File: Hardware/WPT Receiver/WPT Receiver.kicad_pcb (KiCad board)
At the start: 2 copper layers, 100 x 100 mm, 158 parts, among them J1 0.1" Header, J2 Tag-connect-NL, J3 0.1" Header, J4 0.1" Header, SW1 PTS647, SW2 PTS647, SW3 PTS647, U1 STM32G031C6U6, U10 74HC595, U2 INA180A3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

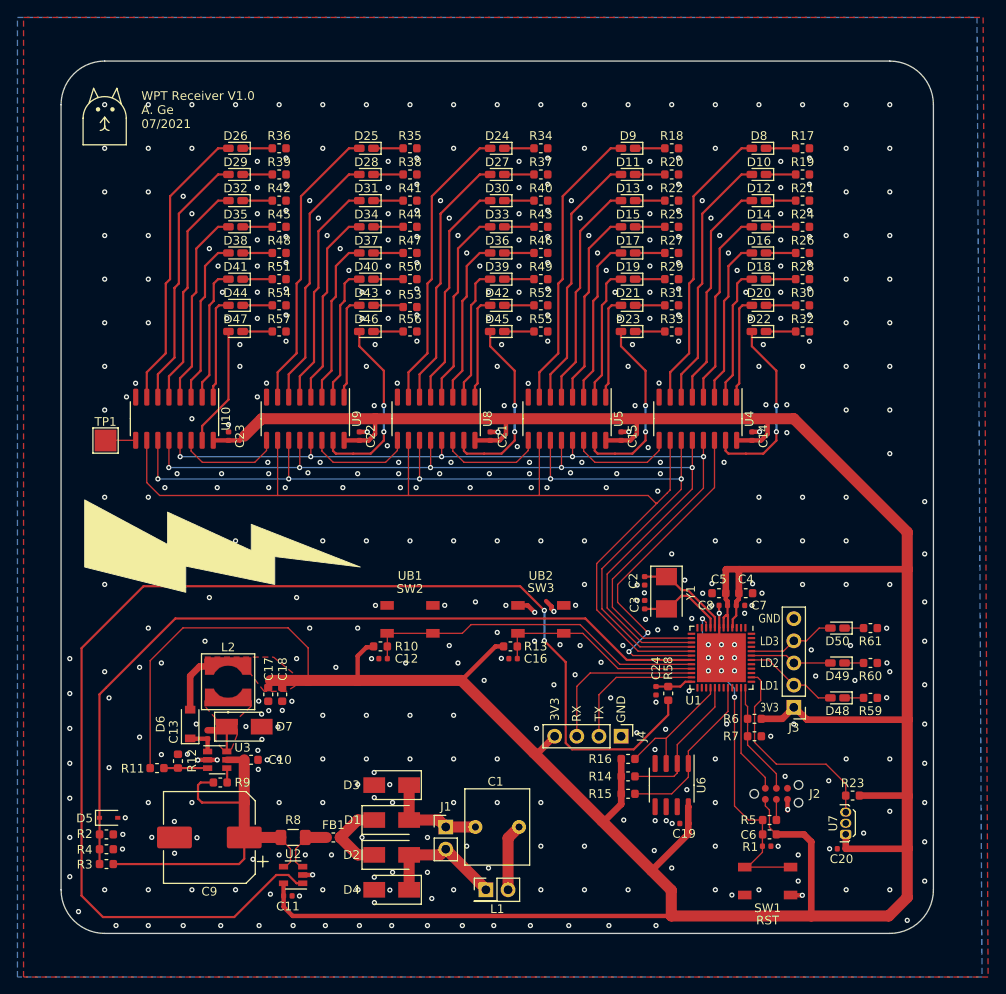
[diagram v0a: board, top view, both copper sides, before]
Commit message: small change to soldermask
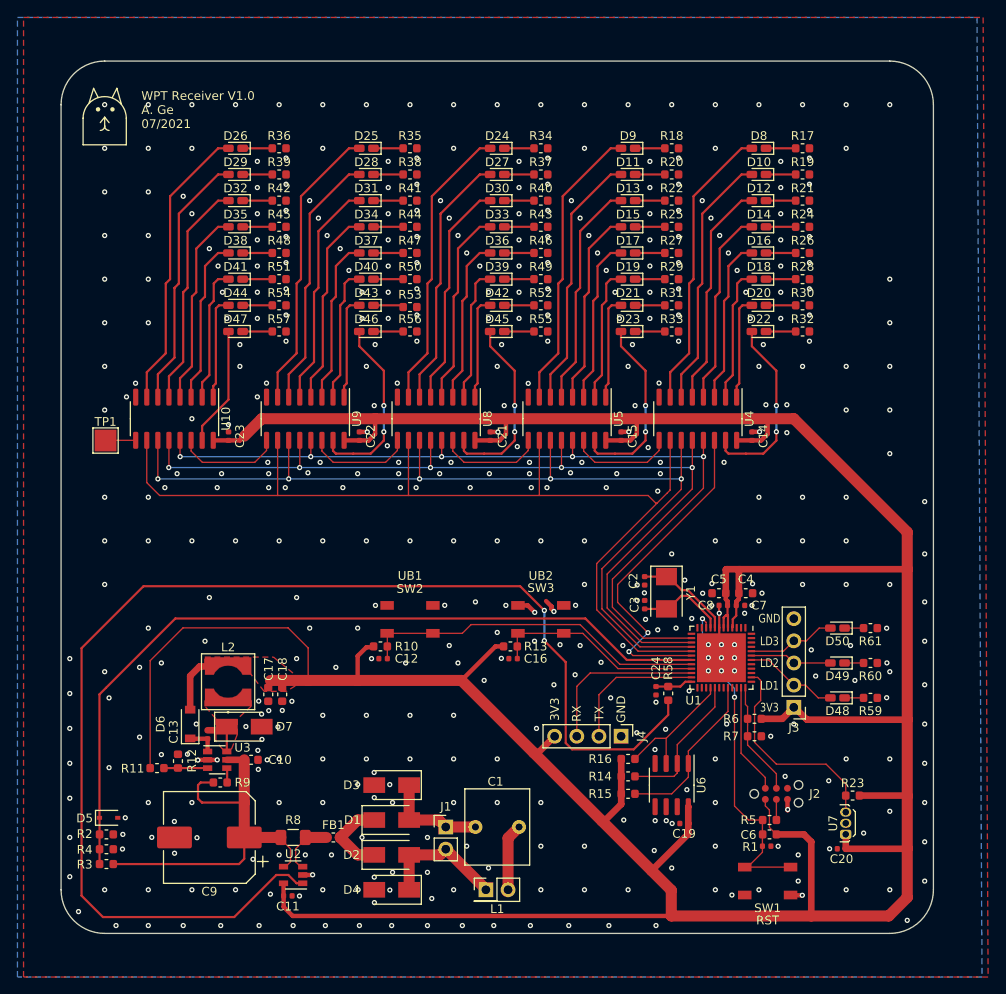
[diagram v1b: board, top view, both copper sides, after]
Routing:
- net GND: vias 466 -> 459
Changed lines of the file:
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@@
     (thickness 1.6)
     (drawings 22)
-    (tracks 1250)
+    (tracks 1243)
     (zones 0)
     (modules 158)
@@
     )
   )
-  (gr_poly (pts (xy 62.2 105.4) (xy 62.2 101.7) (xy 71.8 106.1) (xy 71.8 103.1) (xy 84.3 108) (xy 74.5 106.8) (xy 74.5 110) (xy 64.3 107.9) (xy 64.3 110.9) (xy 52.7 108) (xy 52.7 100.3)) (layer F.SilkS) (width 0.1))
+  (gr_poly (pts (xy 143.6 67) (xy 147.3 67) (xy 142.9 76.6) (xy 145.9 76.6) (xy 141 89.1) (xy 142.2 79.3) (xy 139 79.3) (xy 141.1 69.1) (xy 138.1 69.1) (xy 141 57.5) (xy 148.7 57.5)) (layer F.Mask) (width 0.1))
   (gr_text 3V3 (at 131.2 124.1) (layer F.SilkS)
     (effects (font (size 1 0.8) (thickness 0.15)))
@@
   (via (at 125 60) (size 0.6) (drill 0.3) (layers F.Cu B.Cu) (net 3))
   (via (at 140 60) (size 0.6) (drill 0.3) (layers F.Cu B.Cu) (net 3))
-  (via (at 145 60) (size 0.6) (drill 0.3) (layers F.Cu B.Cu) (net 3))
-  (via (at 145 65) (size 0.6) (drill 0.3) (layers F.Cu B.Cu) (net 3))
-  (via (at 140 65) (size 0.6) (drill 0.3) (layers F.Cu B.Cu) (net 3))
   (via (at 55 70) (size 0.6) (drill 0.3) (layers F.Cu B.Cu) (net 3))
   (via (at 60 70) (size 0.6) (drill 0.3) (layers F.Cu B.Cu) (net 3))
   (via (at 55 75) (size 0.6) (drill 0.3) (layers F.Cu B.Cu) (net 3))
   (via (at 60 75) (size 0.6) (drill 0.3) (layers F.Cu B.Cu) (net 3))
-  (via (at 145 70) (size 0.6) (drill 0.3) (layers F.Cu B.Cu) (net 3))
-  (via (at 140 70) (size 0.6) (drill 0.3) (layers F.Cu B.Cu) (net 3))
   (via (at 145 75) (size 0.6) (drill 0.3) (layers F.Cu B.Cu) (net 3))
-  (via (at 140 75) (size 0.6) (drill 0.3) (layers F.Cu B.Cu) (net 3))
   (via (at 55 80) (size 0.6) (drill 0.3) (layers F.Cu B.Cu) (net 3))
   (via (at 60 80) (size 0.6) (drill 0.3) (layers F.Cu B.Cu) (net 3))
@@
   (via (at 145 85) (size 0.6) (drill 0.3) (layers F.Cu B.Cu) (net 3))
   (via (at 145 80) (size 0.6) (drill 0.3) (layers F.Cu B.Cu) (net 3))
-  (via (at 140 80) (size 0.6) (drill 0.3) (layers F.Cu B.Cu) (net 3))
   (via (at 145 90) (size 0.6) (drill 0.3) (layers F.Cu B.Cu) (net 3))
   (via (at 140 90) (size 0.6) (drill 0.3) (layers F.Cu B.Cu) (net 3))
